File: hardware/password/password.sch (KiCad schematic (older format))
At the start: 69 parts, among them J1 Conn_01x24_Male, J2 Conn_01x24_Male, SW1 SW_DIP_x01, SW10 SW_DIP_x01, SW11 SW_DIP_x01, SW12 SW_DIP_x01, SW13 SW_DIP_x01, SW2 SW_DIP_x01, SW4 SW_DIP_x01, SW5 SW_DIP_x01, SW6 SW_DIP_x01, SW7 SW_DIP_x01, SW8 SW_DIP_x01

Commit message: Create single-board Password PCB
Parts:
- removed D10, D2, D3, D4, D5, D6, D7, D8: D, Diode_THT:D_DO-15_P2.54mm_Vertical_KathodeUp, symbol Device:D
- removed J1, J2: Conn_01x24_Male, Connector_PinHeader_2.54mm:PinHeader_1x24_P2.54mm_Vertical, symbol Connector:Conn_01x24_Male
- removed R1, R2, R3, R4: 1K, Resistor_THT:R_Axial_DIN0309_L9.0mm_D3.2mm_P2.54mm_Vertical, symbol Device:R
- removed R30: 220R, Resistor_THT:R_Axial_DIN0309_L9.0mm_D3.2mm_P2.54mm_Vertical, symbol Device:R
- added C1: 0.1uF, Capacitor_SMD:C_0603_1608Metric_Pad1.05x0.95mm_HandSolder, symbol Device:C
- added D21, D22, D23, D24: D, Diode_SMD:D_0805_2012Metric_Pad1.15x1.40mm_HandSolder, symbol Device:D
- added R28, R29: 220R, Resistor_SMD:R_0603_1608Metric_Pad1.05x0.95mm_HandSolder, symbol Device:R
- added U2: HT1632C-52LQFP, Package_QFP:LQFP-52_14x14mm_P1mm, symbol Driver_LED:HT1632C-52LQFP
- D10: renamed from D1; footprint Diode_THT:D_DO-15_P2.54mm_Vertical_KathodeUp -> Diode_SMD:D_0805_2012Metric_Pad1.15x1.40mm_HandSolder
- D11, D12, D13, D14, D15, D16, D17, D18, D19, D20, D9: footprint Diode_THT:D_DO-15_P2.54mm_Vertical_KathodeUp -> Diode_SMD:D_0805_2012Metric_Pad1.15x1.40mm_HandSolder
- D3: renamed from D21; footprint Package_DIP:DIP-12_W7.62mm_LongPads -> ProjectDisplays:LMD07057BAG
- D4: renamed from D22; footprint Package_DIP:DIP-12_W7.62mm_LongPads -> ProjectDisplays:LMD07057BAG
- D5: renamed from D23; footprint Package_DIP:DIP-12_W7.62mm_LongPads -> ProjectDisplays:LMD07057BAG
- D6: renamed from D24; footprint Package_DIP:DIP-12_W7.62mm_LongPads -> ProjectDisplays:LMD07057BAG
- D7: renamed from D25; footprint Package_DIP:DIP-12_W7.62mm_LongPads -> ProjectDisplays:LMD07057BAG
- R10: renamed from R16; footprint Resistor_THT:R_Axial_DIN0309_L9.0mm_D3.2mm_P2.54mm_Vertical -> Resistor_SMD:R_0603_1608Metric_Pad1.05x0.95mm_HandSolder
- R11: renamed from R21; footprint Resistor_THT:R_Axial_DIN0309_L9.0mm_D3.2mm_P2.54mm_Vertical -> Resistor_SMD:R_0603_1608Metric_Pad1.05x0.95mm_HandSolder
- R12: renamed from R26; footprint Resistor_THT:R_Axial_DIN0309_L9.0mm_D3.2mm_P2.54mm_Vertical -> Resistor_SMD:R_0603_1608Metric_Pad1.05x0.95mm_HandSolder
- R13: renamed from R7; footprint Resistor_THT:R_Axial_DIN0309_L9.0mm_D3.2mm_P2.54mm_Vertical -> Resistor_SMD:R_0603_1608Metric_Pad1.05x0.95mm_HandSolder
- R14: renamed from R12; footprint Resistor_THT:R_Axial_DIN0309_L9.0mm_D3.2mm_P2.54mm_Vertical -> Resistor_SMD:R_0603_1608Metric_Pad1.05x0.95mm_HandSolder
- R15: renamed from R17; footprint Resistor_THT:R_Axial_DIN0309_L9.0mm_D3.2mm_P2.54mm_Vertical -> Resistor_SMD:R_0603_1608Metric_Pad1.05x0.95mm_HandSolder
- R16: renamed from R22; footprint Resistor_THT:R_Axial_DIN0309_L9.0mm_D3.2mm_P2.54mm_Vertical -> Resistor_SMD:R_0603_1608Metric_Pad1.05x0.95mm_HandSolder
- R17: renamed from R27; footprint Resistor_THT:R_Axial_DIN0309_L9.0mm_D3.2mm_P2.54mm_Vertical -> Resistor_SMD:R_0603_1608Metric_Pad1.05x0.95mm_HandSolder
- R18: renamed from R8; footprint Resistor_THT:R_Axial_DIN0309_L9.0mm_D3.2mm_P2.54mm_Vertical -> Resistor_SMD:R_0603_1608Metric_Pad1.05x0.95mm_HandSolder
- R19: renamed from R13; footprint Resistor_THT:R_Axial_DIN0309_L9.0mm_D3.2mm_P2.54mm_Vertical -> Resistor_SMD:R_0603_1608Metric_Pad1.05x0.95mm_HandSolder
- R20: renamed from R18; footprint Resistor_THT:R_Axial_DIN0309_L9.0mm_D3.2mm_P2.54mm_Vertical -> Resistor_SMD:R_0603_1608Metric_Pad1.05x0.95mm_HandSolder
- R21: renamed from R23; footprint Resistor_THT:R_Axial_DIN0309_L9.0mm_D3.2mm_P2.54mm_Vertical -> Resistor_SMD:R_0603_1608Metric_Pad1.05x0.95mm_HandSolder
- R22: renamed from R28; footprint Resistor_THT:R_Axial_DIN0309_L9.0mm_D3.2mm_P2.54mm_Vertical -> Resistor_SMD:R_0603_1608Metric_Pad1.05x0.95mm_HandSolder
- R23: renamed from R9; footprint Resistor_THT:R_Axial_DIN0309_L9.0mm_D3.2mm_P2.54mm_Vertical -> Resistor_SMD:R_0603_1608Metric_Pad1.05x0.95mm_HandSolder
- R24: renamed from R14; footprint Resistor_THT:R_Axial_DIN0309_L9.0mm_D3.2mm_P2.54mm_Vertical -> Resistor_SMD:R_0603_1608Metric_Pad1.05x0.95mm_HandSolder
- R25: renamed from R19; footprint Resistor_THT:R_Axial_DIN0309_L9.0mm_D3.2mm_P2.54mm_Vertical -> Resistor_SMD:R_0603_1608Metric_Pad1.05x0.95mm_HandSolder
- R26: renamed from R24; footprint Resistor_THT:R_Axial_DIN0309_L9.0mm_D3.2mm_P2.54mm_Vertical -> Resistor_SMD:R_0603_1608Metric_Pad1.05x0.95mm_HandSolder
- R27: renamed from R29; footprint Resistor_THT:R_Axial_DIN0309_L9.0mm_D3.2mm_P2.54mm_Vertical -> Resistor_SMD:R_0603_1608Metric_Pad1.05x0.95mm_HandSolder
- R3: renamed from R5; footprint Resistor_THT:R_Axial_DIN0309_L9.0mm_D3.2mm_P2.54mm_Vertical -> Resistor_SMD:R_0603_1608Metric_Pad1.05x0.95mm_HandSolder
- R4: renamed from R10; footprint Resistor_THT:R_Axial_DIN0309_L9.0mm_D3.2mm_P2.54mm_Vertical -> Resistor_SMD:R_0603_1608Metric_Pad1.05x0.95mm_HandSolder
- R5: renamed from R15; footprint Resistor_THT:R_Axial_DIN0309_L9.0mm_D3.2mm_P2.54mm_Vertical -> Resistor_SMD:R_0603_1608Metric_Pad1.05x0.95mm_HandSolder
- R6: renamed from R20; footprint Resistor_THT:R_Axial_DIN0309_L9.0mm_D3.2mm_P2.54mm_Vertical -> Resistor_SMD:R_0603_1608Metric_Pad1.05x0.95mm_HandSolder
- R7: renamed from R25; footprint Resistor_THT:R_Axial_DIN0309_L9.0mm_D3.2mm_P2.54mm_Vertical -> Resistor_SMD:R_0603_1608Metric_Pad1.05x0.95mm_HandSolder
- R8: renamed from R6; footprint Resistor_THT:R_Axial_DIN0309_L9.0mm_D3.2mm_P2.54mm_Vertical -> Resistor_SMD:R_0603_1608Metric_Pad1.05x0.95mm_HandSolder
- R9: renamed from R11; footprint Resistor_THT:R_Axial_DIN0309_L9.0mm_D3.2mm_P2.54mm_Vertical -> Resistor_SMD:R_0603_1608Metric_Pad1.05x0.95mm_HandSolder
- SW1: footprint Package_DIP:DIP-4_W7.62mm_LongPads -> Button_Switch_SMD:SW_Push_1P1T_NO_6x6mm_H9.5mm
- SW10: renamed from SW12; footprint Package_DIP:DIP-4_W7.62mm_LongPads -> Button_Switch_SMD:SW_Push_1P1T_NO_6x6mm_H9.5mm
- SW11: renamed from SW13; footprint Package_DIP:DIP-4_W7.62mm_LongPads -> Button_Switch_SMD:SW_Push_1P1T_NO_6x6mm_H9.5mm
- SW2: renamed from SW7; footprint Package_DIP:DIP-4_W7.62mm_LongPads -> Button_Switch_SMD:SW_Push_1P1T_NO_6x6mm_H9.5mm
- SW3: renamed from SW2; footprint Package_DIP:DIP-4_W7.62mm_LongPads -> Button_Switch_SMD:SW_Push_1P1T_NO_6x6mm_H9.5mm
- SW4: renamed from SW8; footprint Package_DIP:DIP-4_W7.62mm_LongPads -> Button_Switch_SMD:SW_Push_1P1T_NO_6x6mm_H9.5mm
- SW5: renamed from SW4; footprint Package_DIP:DIP-4_W7.62mm_LongPads -> Button_Switch_SMD:SW_Push_1P1T_NO_6x6mm_H9.5mm
- SW6: renamed from SW10; footprint Package_DIP:DIP-4_W7.62mm_LongPads -> Button_Switch_SMD:SW_Push_1P1T_NO_6x6mm_H9.5mm
- SW7: renamed from SW5; footprint Package_DIP:DIP-4_W7.62mm_LongPads -> Button_Switch_SMD:SW_Push_1P1T_NO_6x6mm_H9.5mm
- SW8: renamed from SW11; footprint Package_DIP:DIP-4_W7.62mm_LongPads -> Button_Switch_SMD:SW_Push_1P1T_NO_6x6mm_H9.5mm
- SW9: renamed from SW6; footprint Package_DIP:DIP-4_W7.62mm_LongPads -> Button_Switch_SMD:SW_Push_1P1T_NO_6x6mm_H9.5mm
- renumbered D26 to D8
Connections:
- net labels added: A0, A1, A6, D10, D3, D4, D5, D6, D7, D9, GND
- wire segments 337 -> 318
- no-connect marks 0 -> 12
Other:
- moved on the sheet: D10, D3, D4, D5, D6, D7, D8, R10, R11, R12, R13, R14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

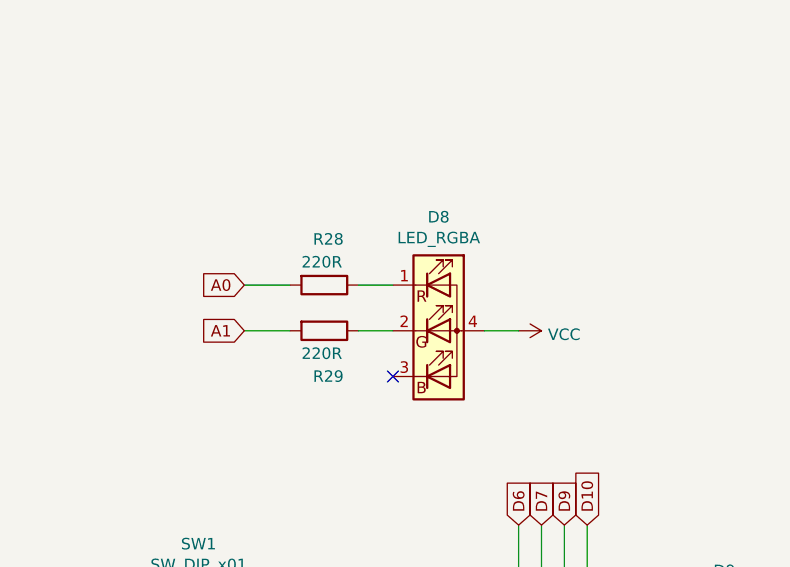
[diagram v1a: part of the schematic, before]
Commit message: Password PCB: switch to correct RGB LED symbol
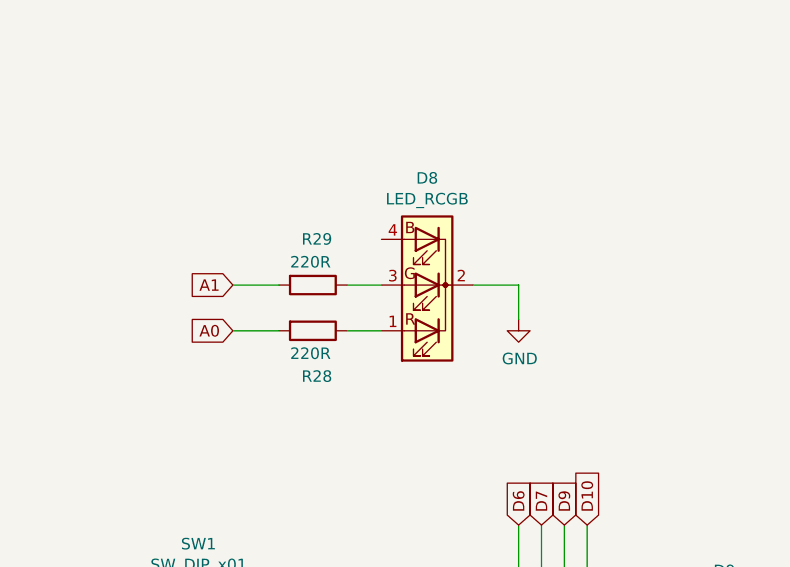
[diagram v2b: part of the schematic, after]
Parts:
- removed D8: LED_RGBA, LED_THT:LED_D5.0mm-4_RGB_Wide_Pins, symbol Device:LED_RGBA
- added D8: LED_RCGB, LED_THT:LED_D5.0mm-4_RGB_Wide_Pins, symbol Device:LED_RCGB
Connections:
- net GND: now also D8.2 (K)
- net at R28.1: now also D8.1 (RA)
- net at R29.1: now also D8.3 (GA)
- no-connect marks 12 -> 11
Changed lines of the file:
@@
 Wire Wire Line
 	4150 10500 4250 10500
-$Comp
-L power:VCC #PWR014
-U 1 1 5E626A27
-P 2950 6950
-F 0 "#PWR014" H 2950 6800 50  0001 C CNN
-F 1 "VCC" V 2967 7078 50  0000 L CNN
-F 2 "" H 2950 6950 50  0001 C CNN
-F 3 "" H 2950 6950 50  0001 C CNN
-	1    2950 6950
-	0    1    1    0
-$EndComp
 Wire Wire Line
 	4850 10500 4850 9950
@@
 	1850 9050 2150 9050
 Connection ~ 4150 9050
-$Comp
-L Device:LED_RGBA D8
-U 1 1 5E8061C6
-P 2600 6950
-F 0 "D8" H 2600 7447 50  0000 C CNN
-F 1 "LED_RGBA" H 2600 7356 50  0000 C CNN
-F 2 "LED_THT:LED_D5.0mm-4_RGB_Wide_Pins" H 2600 6900 50  0001 C CNN
-F 3 "~" H 2600 6900 50  0001 C CNN
-	1    2600 6950
-	1    0    0    -1
-$EndComp
 $Sheet
 S 1050 1000 2150 250
@@
 	4800 6550 4800 5950
 Connection ~ 4800 5950
-Wire Wire Line
-	2400 6750 2250 6750
-Wire Wire Line
-	2250 6950 2400 6950
-$Comp
-L Device:R R28
-U 1 1 5FF4334D
-P 2100 6750
-F 0 "R28" V 1900 6700 50  0000 L CNN
-F 1 "220R" V 2000 6650 50  0000 L CNN
-F 2 "Resistor_SMD:R_0603_1608Metric_Pad1.05x0.95mm_HandSolder" V 2030 6750 50  0001 C CNN
-F 3 "~" H 2100 6750 50  0001 C CNN
-	1    2100 6750
-	0    1    1    0
-$EndComp
-$Comp
-L Device:R R29
-U 1 1 5FF44364
-P 2100 6950
-F 0 "R29" V 2300 6900 50  0000 L CNN
-F 1 "220R" V 2200 6850 50  0000 L CNN
-F 2 "Resistor_SMD:R_0603_1608Metric_Pad1.05x0.95mm_HandSolder" V 2030 6950 50  0001 C CNN
-F 3 "~" H 2100 6950 50  0001 C CNN
-	1    2100 6950
-	0    1    1    0
-$EndComp
-Wire Wire Line
-	1750 6950 1950 6950
-Wire Wire Line
-	1950 6750 1750 6750
-NoConn ~ 2400 7150
-Wire Wire Line
-	2950 6950 2800 6950
 Text GLabel 12200 2650 2    50   Input ~ 0
 D5
@@
 Text GLabel 4150 10500 0    50   Input ~ 0
 A6
-Text GLabel 1750 6950 0    50   Input ~ 0
-A1
-Text GLabel 1750 6750 0    50   Input ~ 0
-A0
 Wire Wire Line
 	2450 8150 2950 8150
@@
 Wire Wire Line
 	6250 3100 6850 3100
+Text GLabel 1700 6950 0    50   Input ~ 0
+A0
+Text GLabel 1700 6750 0    50   Input ~ 0
+A1
+Wire Wire Line
+	1900 6750 1700 6750
+Wire Wire Line
+	1700 6950 1900 6950
+$Comp
+L Device:R R28
+U 1 1 5F759493
+P 2050 6950
+F 0 "R28" V 2250 6900 50  0000 L CNN
+F 1 "220R" V 2150 6850 50  0000 L CNN
+F 2 "Resistor_SMD:R_0603_1608Metric_Pad1.05x0.95mm_HandSolder" V 1980 6950 50  0001 C CNN
+F 3 "~" H 2050 6950 50  0001 C CNN
+	1    2050 6950
+	0    1    1    0
+$EndComp
+$Comp
+L Device:R R29
+U 1 1 5F75948D
+P 2050 6750
+F 0 "R29" V 1850 6700 50  0000 L CNN
+F 1 "220R" V 1950 6650 50  0000 L CNN
+F 2 "Resistor_SMD:R_0603_1608Metric_Pad1.05x0.95mm_HandSolder" V 1980 6750 50  0001 C CNN
+F 3 "~" H 2050 6750 50  0001 C CNN
+	1    2050 6750
+	0    1    1    0
+$EndComp
+Wire Wire Line
+	2200 6950 2350 6950
+Wire Wire Line
+	2350 6750 2200 6750
+Wire Wire Line
+	2950 6750 2950 6900
+Wire Wire Line
+	2750 6750 2950 6750
+$Comp
+L power:GND #PWR?
+U 1 1 5F73BAE5
+P 2950 6900
+F 0 "#PWR?" H 2950 6650 50  0001 C CNN
+F 1 "GND" H 2955 6727 50  0000 C CNN
+F 2 "" H 2950 6900 50  0001 C CNN
+F 3 "" H 2950 6900 50  0001 C CNN
+	1    2950 6900
+	1    0    0    -1
+$EndComp
+$Comp
+L Device:LED_RCGB D8
+U 1 1 5F7036D4
+P 2550 6750
+F 0 "D8" H 2550 6283 50  0000 C CNN
+F 1 "LED_RCGB" H 2550 6374 50  0000 C CNN
+F 2 "LED_THT:LED_D5.0mm-4_RGB_Wide_Pins" H 2550 6700 50  0001 C CNN
+F 3 "~" H 2550 6700 50  0001 C CNN
+	1    2550 6750
+	-1   0    0    1
+$EndComp
 $EndSCHEMATC

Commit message: Clean up symbol libraries, delete outdated files
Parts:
- D3, D4, D5, D6, D7: value 7x5LedMatrix -> LMD07057BAG; symbol 7x5matrix:7x5LedMatrix -> ProjectDisplays:LMD07057BAG
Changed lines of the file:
@@
 Connection ~ 4850 9500
 $Comp
-L 7x5matrix:7x5LedMatrix D4
+L ProjectDisplays:LMD07057BAG D4
 U 1 1 5DEC2CC5
 P 5500 1900
 F 0 "D4" H 5500 1865 50  0000 C CNN
-F 1 "7x5LedMatrix" H 5500 1774 50  0000 C CNN
+F 1 "LMD07057BAG" H 5500 1774 50  0000 C CNN
 F 2 "ProjectDisplays:LMD07057BAG" H 5500 1900 50  0001 C CNN
 F 3 "" H 5500 1900 50  0001 C CNN
@@
 $EndComp
 $Comp
-L 7x5matrix:7x5LedMatrix D3
+L ProjectDisplays:LMD07057BAG D3
 U 1 1 5DEC6397
 P 5500 850
 F 0 "D3" H 5500 815 50  0000 C CNN
-F 1 "7x5LedMatrix" H 5500 724 50  0000 C CNN
+F 1 "LMD07057BAG" H 5500 724 50  0000 C CNN
 F 2 "ProjectDisplays:LMD07057BAG" H 5500 850 50  0001 C CNN
 F 3 "" H 5500 850 50  0001 C CNN
@@
 $EndComp
 $Comp
-L 7x5matrix:7x5LedMatrix D5
+L ProjectDisplays:LMD07057BAG D5
 U 1 1 5DEC73BF
 P 5500 2950
 F 0 "D5" H 5500 2915 50  0000 C CNN
-F 1 "7x5LedMatrix" H 5500 2824 50  0000 C CNN
+F 1 "LMD07057BAG" H 5500 2824 50  0000 C CNN
 F 2 "ProjectDisplays:LMD07057BAG" H 5500 2950 50  0001 C CNN
 F 3 "" H 5500 2950 50  0001 C CNN
@@
 $EndComp
 $Comp
-L 7x5matrix:7x5LedMatrix D6
+L ProjectDisplays:LMD07057BAG D6
 U 1 1 5DEC821B
 P 5500 4000
 F 0 "D6" H 5500 3965 50  0000 C CNN
-F 1 "7x5LedMatrix" H 5500 3874 50  0000 C CNN
+F 1 "LMD07057BAG" H 5500 3874 50  0000 C CNN
 F 2 "ProjectDisplays:LMD07057BAG" H 5500 4000 50  0001 C CNN
 F 3 "" H 5500 4000 50  0001 C CNN
@@
 $EndComp
 $Comp
-L 7x5matrix:7x5LedMatrix D7
+L ProjectDisplays:LMD07057BAG D7
 U 1 1 5DEC9199
 P 5500 5050
 F 0 "D7" H 5500 5015 50  0000 C CNN
-F 1 "7x5LedMatrix" H 5500 4924 50  0000 C CNN
+F 1 "LMD07057BAG" H 5500 4924 50  0000 C CNN
 F 2 "ProjectDisplays:LMD07057BAG" H 5500 5050 50  0001 C CNN
 F 3 "" H 5500 5050 50  0001 C CNN

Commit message: Password PCB: change display polarity
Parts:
- removed R10, R11, R12, R13, R14, R15, R16, R17, R18, R19, R20, R21, R22, R23, R24, R25, R26, R27, R4, R5, R6, R7, R8, R9: 220R, Resistor_SMD:R_0603_1608Metric_Pad1.05x0.95mm_HandSolder, symbol Device:R
- added R10, R11, R12, R13, R14, R15, R16, R4, R5, R6, R7, R8, R9: 82R, Resistor_SMD:R_0603_1608Metric_Pad0.98x0.95mm_HandSolder, symbol Device:R_Small
- R28, R29: value 220R -> 82R; footprint Resistor_SMD:R_0603_1608Metric_Pad1.05x0.95mm_HandSolder -> Resistor_SMD:R_0603_1608Metric_Pad0.98x0.95mm_HandSolder
- R3: value 220R -> 82R; footprint Resistor_SMD:R_0603_1608Metric_Pad1.05x0.95mm_HandSolder -> Resistor_SMD:R_0603_1608Metric_Pad0.98x0.95mm_HandSolder; symbol Device:R -> Device:R_Small
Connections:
- net COL6: now reaches D4.1 (COL1)
- net COL6: now also D7.1 (COL1), U2.28 (COM5)
- net COL8: now reaches D4.10 (COL3)
- net COL8: now also D7.10 (COL3), U2.32 (ROW30/COM9)
- net ROW2L: now reaches D3.11 (ROW2), D4.11 (ROW2), D5.11 (ROW2)
- net ROW2L: now also R8.1; no longer D6.11 (ROW2), D7.11 (ROW2), U2.23 (COM1)
- net ROW1L: now reaches D3.12 (ROW1), D4.12 (ROW1), D5.12 (ROW1)
- net ROW1L: now also R9.1; no longer D6.12 (ROW1), D7.12 (ROW1), U2.22 (COM0)
- net ROW3L: now reaches D3.2 (ROW3), D4.2 (ROW3), D5.2 (ROW3)
- net ROW3L: now also R3.1; no longer D6.2 (ROW3), D7.2 (ROW3), U2.24 (COM2)
- net COL7: now reaches D4.3 (COL2)
- net COL7: now also D7.3 (COL2), U2.29 (COM6)
- net ROW5L: now reaches D3.4 (ROW5), D4.4 (ROW5), D5.4 (ROW5)
- net ROW5L: now also R4.1; no longer D6.4 (ROW5), D7.4 (ROW5), U2.27 (COM4)
- net ROW6L: now reaches D3.5 (ROW6), D4.5 (ROW6), D5.5 (ROW6)
- net ROW6L: now also R5.1; no longer D6.5 (ROW6), D7.5 (ROW6), U2.28 (COM5)
- net ROW7L: now reaches D3.6 (ROW7), D4.6 (ROW7), D5.6 (ROW7)
- net ROW7L: now also R6.1; no longer D6.6 (ROW7), D7.6 (ROW7), U2.29 (COM6)
- net COL9: now reaches D4.7 (COL4)
- net COL9: now also D7.7 (COL4), U2.30 (COM7)
- net COL10: now reaches D4.8 (COL5)
- net COL10: now also D7.8 (COL5), U2.31 (ROW31/COM8)
- net ROW4L: now reaches D3.9 (ROW4), D4.9 (ROW4), D5.9 (ROW4)
- net ROW4L: now also R7.1; no longer D6.9 (ROW4), D7.9 (ROW4), U2.26 (COM3)
- net COL1: now reaches D3.1 (COL1)
- net COL1: now also U2.33 (ROW29/COM10)
- net COL3: now reaches D3.10 (COL3)
- net COL3: now also U2.39 (ROW25/COM14)
- net COL2: now reaches D3.3 (COL2)
- net COL2: now also U2.34 (ROW28/COM11)
- net COL4: now reaches D3.7 (COL4)
- net COL4: now also U2.35 (ROW27/COM12)
- net at R3.2: now also U2.13 (ROW0); no longer D3.8 (COL5)
- net COL11: now reaches D5.1 (COL1)
- net COL11: now also D6.1 (COL1), U2.22 (COM0)
- net COL13: now reaches D5.10 (COL3)
- net COL13: now also D6.10 (COL3), U2.27 (COM4)
- net COL12: now reaches D5.3 (COL2)
- net COL12: now also D6.3 (COL2), U2.23 (COM1)
- net COL14: now reaches D5.7 (COL4)
- net COL14: now also D6.7 (COL4), U2.24 (COM2)
- net COL15: now reaches D5.8 (COL5)
- net COL15: now also D6.8 (COL5), U2.26 (COM3)
- net at U2.10 (ROW3): now also R6.2; no longer R3.1
- net at U2.11 (ROW2): now also R5.2
- net at U2.9 (ROW4): now also R7.2
- net at U2.12 (ROW1): now also R4.2
- net at U2.4 (ROW8): now also R11.2
- net at U2.5 (ROW7): now also R10.2
- net at U2.3 (ROW9): now also R12.2
- net at U2.6 (ROW6): now also R9.2
- net at U2.8 (ROW5): now also R8.2
- net at U2.51 (ROW13): now also R16.2
- net at U2.52 (ROW12): now also R15.2
- net at U2.1 (ROW11): now also R14.2
- net at U2.2 (ROW10): now also R13.2
- net COL5: now reaches U2.37 (ROW26/COM13)
- net COL5: now also D3.8 (COL5)
- new net ROW1R: D6.12 (ROW1), D7.12 (ROW1), R16.1
- new net ROW2R: D6.11 (ROW2), D7.11 (ROW2), R15.1
- new net ROW3R: D6.2 (ROW3), D7.2 (ROW3), R10.1
- new net ROW4R: D6.9 (ROW4), D7.9 (ROW4), R14.1
- new net ROW5R: D6.4 (ROW5), D7.4 (ROW5), R11.1
- new net ROW6R: D6.5 (ROW6), D7.5 (ROW6), R12.1
- new net ROW7R: D6.6 (ROW7), D7.6 (ROW7), R13.1
- no-connect marks 11 -> 3
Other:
- moved on the sheet: C1, D3, D4, D5, D6, D7, R3, U2

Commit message: Password PCB: swap ADC-only pin A6 for A5
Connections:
- net A6 renamed A5_SCL
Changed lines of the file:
@@
 	3250 7800 3250 8500
 Text GLabel 4150 10500 0    50   Input ~ 0
-A6
+A5_SCL
 Wire Wire Line
 	2450 8150 2950 8150

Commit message: Avoid using D10 (SPI SS) pin as input
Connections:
- net D10 renamed A4_SDA
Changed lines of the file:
@@
 	3150 8050 3150 7800
 Text GLabel 3250 7800 1    50   Input ~ 0
-D10
+A4_SDA
 Text GLabel 3150 7800 1    50   Input ~ 0
 D9
